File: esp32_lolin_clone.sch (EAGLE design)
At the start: 33 parts, among them J1 10104111-0001LF, P1 S2B-PH-SM4-TB, Q1 CJ2301S1, Q2 CJ2301S1, SW1 PTS815SJK250SMTR, U1 ESP32-WROOM-32D, U2 BCM857, U3 ME6211, U4 UMH3N, U5 TP4054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

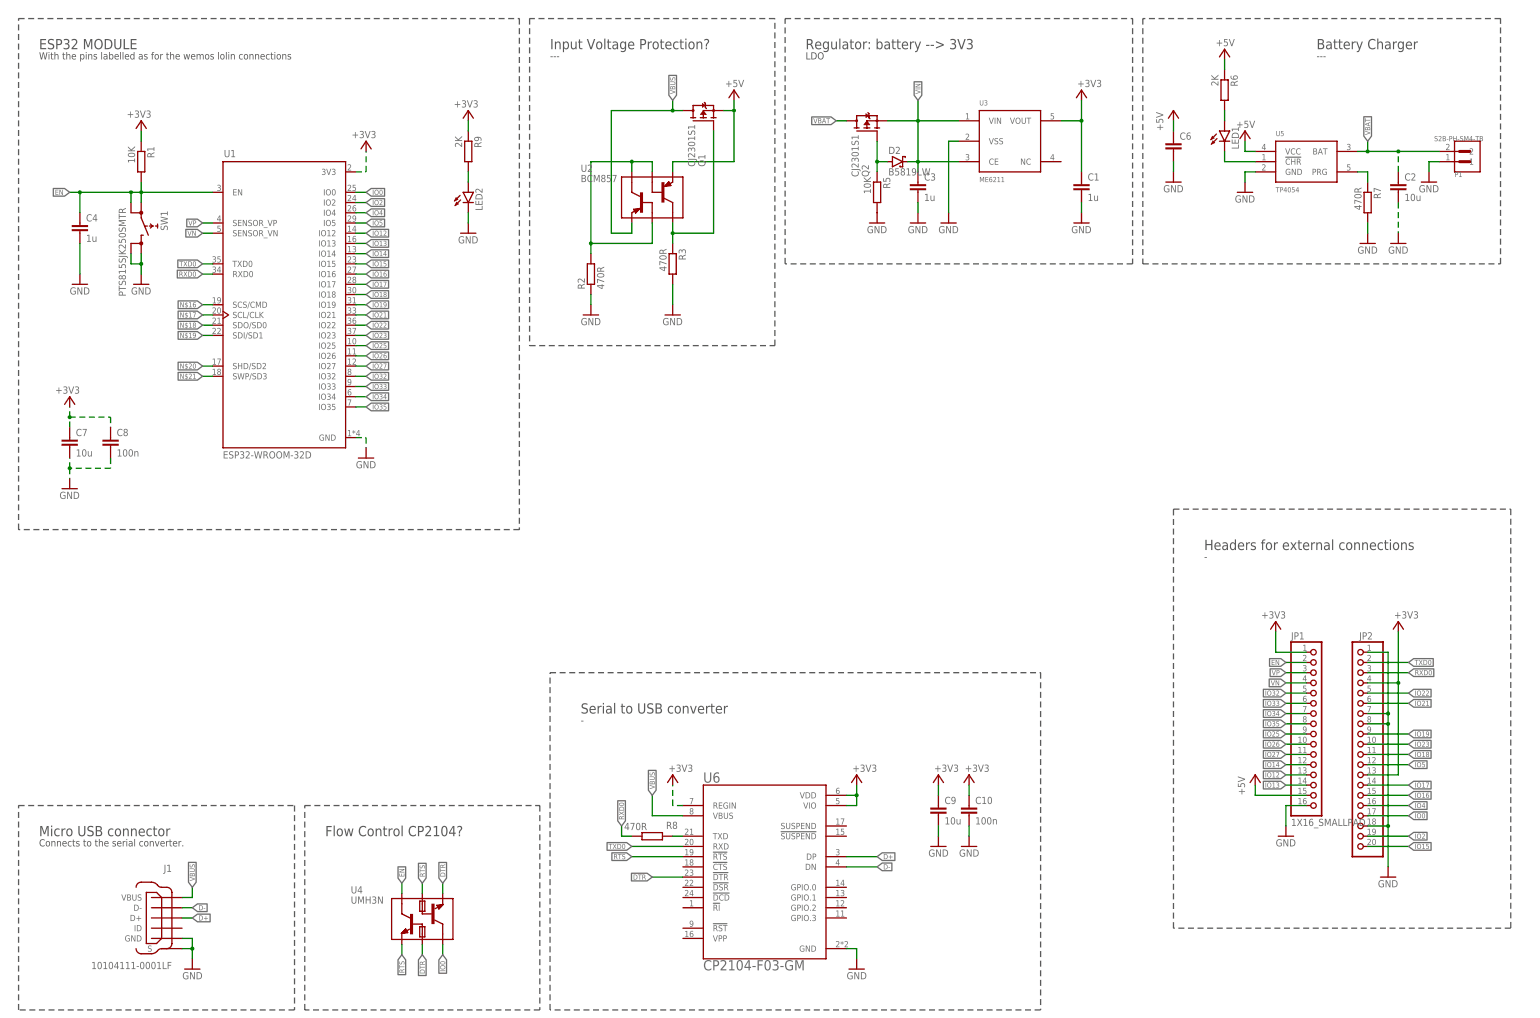
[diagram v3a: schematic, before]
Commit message: - Finish BOM, modify BOM related issues in schematic.
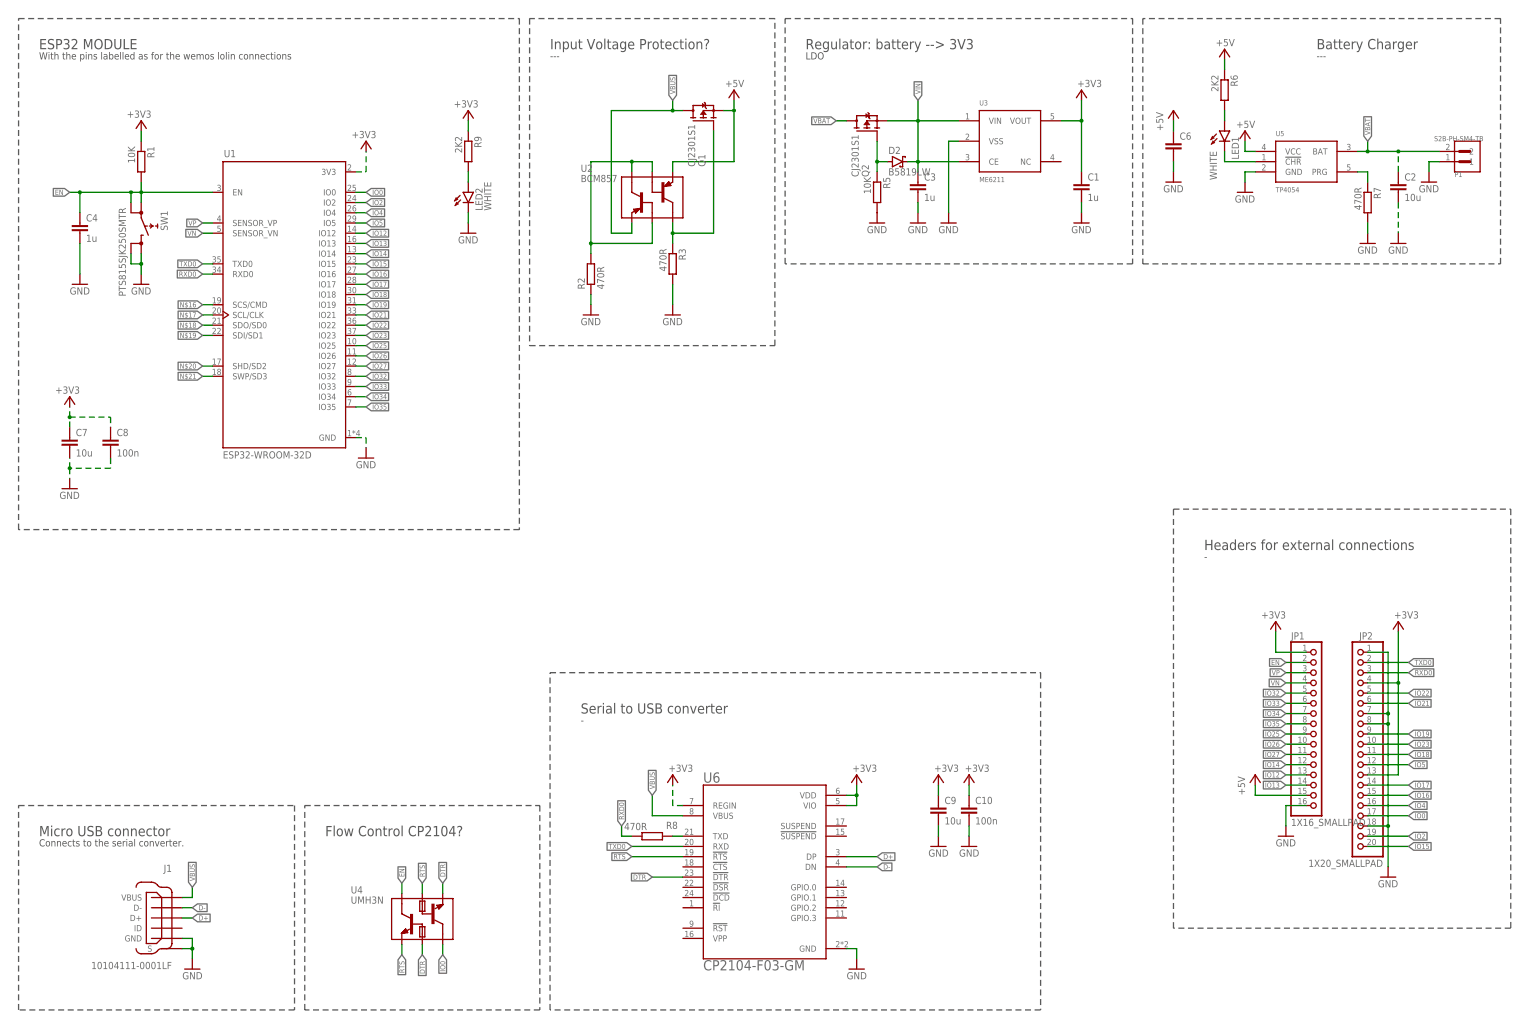
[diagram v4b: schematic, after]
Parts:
- JP2: value (none) -> 1X20_SMALLPAD; device RE_wemos_lolin_clone:PINHD-1X20 -> RE_wemos_lolin_clone:1X20_SMALLPAD
- LED1, LED2: value (none) -> WHITE
- R6, R9: value 2K -> 2K2
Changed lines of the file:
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@@
 <part name="U6" library="RE_wemos_lolin_clone" deviceset="CP2104" device="-F03-GM"/>
 <part name="R8" library="rcl" library_urn="urn:adsk.eagle:library:334" deviceset="R-EU_" device="R0603" package3d_urn="urn:adsk.eagle:package:23555/3" value="470R"/>
-<part name="LED2" library="led" library_urn="urn:adsk.eagle:library:259" deviceset="LED" device="CHIP-LED0603" package3d_urn="urn:adsk.eagle:package:15819/3"/>
-<part name="R9" library="rcl" library_urn="urn:adsk.eagle:library:334" deviceset="R-EU_" device="R0603" package3d_urn="urn:adsk.eagle:package:23555/3" value="2K"/>
+<part name="LED2" library="led" library_urn="urn:adsk.eagle:library:259" deviceset="LED" device="CHIP-LED0603" package3d_urn="urn:adsk.eagle:package:15819/3" value="WHITE"/>
+<part name="R9" library="rcl" library_urn="urn:adsk.eagle:library:334" deviceset="R-EU_" device="R0603" package3d_urn="urn:adsk.eagle:package:23555/3" value="2K2"/>
 <part name="GND1" library="supply1" library_urn="urn:adsk.eagle:library:371" deviceset="GND" device=""/>
 <part name="+3V1" library="supply1" library_urn="urn:adsk.eagle:library:371" deviceset="+3V3" device=""/>
 <part name="C10" library="rcl" library_urn="urn:adsk.eagle:library:334" deviceset="C-EU" device="C0603K" package3d_urn="urn:adsk.eagle:package:23680/2" value="100n"/>
 <part name="JP1" library="RE_wemos_lolin_clone" deviceset="1X16_SMALLPAD" device=""/>
-<part name="JP2" library="RE_wemos_lolin_clone" deviceset="PINHD-1X20" device="" package3d_urn="urn:adsk.eagle:package:22441/2"/>
+<part name="JP2" library="RE_wemos_lolin_clone" deviceset="1X20_SMALLPAD" device=""/>
 <part name="GND2" library="supply1" library_urn="urn:adsk.eagle:library:371" deviceset="GND" device=""/>
 <part name="+3V2" library="supply1" library_urn="urn:adsk.eagle:library:371" deviceset="+3V3" device=""/>
@@
 <part name="GND15" library="supply1" library_urn="urn:adsk.eagle:library:371" deviceset="GND" device=""/>
 <part name="+3V7" library="supply1" library_urn="urn:adsk.eagle:library:371" deviceset="+3V3" device=""/>
-<part name="LED1" library="led" library_urn="urn:adsk.eagle:library:259" deviceset="LED" device="CHIP-LED0603" package3d_urn="urn:adsk.eagle:package:15819/3"/>
-<part name="R6" library="rcl" library_urn="urn:adsk.eagle:library:334" deviceset="R-EU_" device="R0603" package3d_urn="urn:adsk.eagle:package:23555/3" value="2K"/>
+<part name="LED1" library="led" library_urn="urn:adsk.eagle:library:259" deviceset="LED" device="CHIP-LED0603" package3d_urn="urn:adsk.eagle:package:15819/3" value="WHITE"/>
+<part name="R6" library="rcl" library_urn="urn:adsk.eagle:library:334" deviceset="R-EU_" device="R0603" package3d_urn="urn:adsk.eagle:package:23555/3" value="2K2"/>
 <part name="P+3" library="supply1" library_urn="urn:adsk.eagle:library:371" deviceset="+5V" device=""/>
 <part name="GND16" library="supply1" library_urn="urn:adsk.eagle:library:371" deviceset="GND" device=""/>
@@
 <attribute name="VALUE" x="323.85" y="53.34" size="1.778" layer="96"/>
 </instance>
-<instance part="JP2" gate="A" x="340.36" y="73.66" smashed="yes" rot="MR0">
+<instance part="JP2" gate="G$1" x="340.36" y="73.66" smashed="yes" rot="MR0">
 <attribute name="NAME" x="344.17" y="99.695" size="1.778" layer="95" rot="MR0"/>
 <attribute name="VALUE" x="346.71" y="43.18" size="1.778" layer="96" rot="MR0"/>
@@
 </instance>
 <instance part="LED1" gate="G$1" x="307.34" y="226.06" smashed="yes">
-<attribute name="NAME" x="310.896" y="221.488" size="1.778" layer="95" rot="R90"/>
-<attribute name="VALUE" x="313.055" y="221.488" size="1.778" layer="96" rot="R90"/>
+<attribute name="NAME" x="310.896" y="218.948" size="1.778" layer="95" rot="R90"/>
+<attribute name="VALUE" x="305.435" y="213.868" size="1.778" layer="96" rot="R90"/>
 </instance>
 <instance part="R6" gate="G$1" x="307.34" y="236.22" smashed="yes" rot="R270">
@@
 </segment>
 <segment>
-<pinref part="JP2" gate="A" pin="2"/>
+<pinref part="JP2" gate="G$1" pin="2"/>
 <wire x1="342.9" y1="93.98" x2="353.06" y2="93.98" width="0.1524" layer="91"/>
 <label x="353.06" y="93.98" size="1.27" layer="95" xref="yes"/>
@@
 </segment>
 <segment>
-<pinref part="JP2" gate="A" pin="3"/>
+<pinref part="JP2" gate="G$1" pin="3"/>
 <wire x1="342.9" y1="91.44" x2="353.06" y2="91.44" width="0.1524" layer="91"/>
 <label x="353.06" y="91.44" size="1.27" layer="95" xref="yes"/>
@@
 </segment>
 <segment>
-<pinref part="JP2" gate="A" pin="4"/>
+<pinref part="JP2" gate="G$1" pin="4"/>
 <wire x1="342.9" y1="88.9" x2="350.52" y2="88.9" width="0.1524" layer="91"/>
 <wire x1="350.52" y1="88.9" x2="350.52" y2="101.6" width="0.1524" layer="91"/>
-<pinref part="JP2" gate="A" pin="13"/>
+<pinref part="JP2" gate="G$1" pin="13"/>
 <wire x1="342.9" y1="66.04" x2="350.52" y2="66.04" width="0.1524" layer="91"/>
 <wire x1="350.52" y1="66.04" x2="350.52" y2="88.9" width="0.1524" layer="91"/>
@@
 </segment>
 <segment>
-<pinref part="JP2" gate="A" pin="1"/>
+<pinref part="JP2" gate="G$1" pin="1"/>
 <wire x1="342.9" y1="96.52" x2="347.98" y2="96.52" width="0.1524" layer="91"/>
 <pinref part="GND3" gate="1" pin="GND"/>
 <wire x1="347.98" y1="96.52" x2="347.98" y2="81.28" width="0.1524" layer="91"/>
-<pinref part="JP2" gate="A" pin="7"/>
+<pinref part="JP2" gate="G$1" pin="7"/>
 <wire x1="347.98" y1="81.28" x2="347.98" y2="78.74" width="0.1524" layer="91"/>
 <wire x1="347.98" y1="78.74" x2="347.98" y2="53.34" width="0.1524" layer="91"/>
@@
 <wire x1="342.9" y1="81.28" x2="347.98" y2="81.28" width="0.1524" layer="91"/>
 <junction x="347.98" y="81.28"/>
-<pinref part="JP2" gate="A" pin="8"/>
+<pinref part="JP2" gate="G$1" pin="8"/>
 <wire x1="342.9" y1="78.74" x2="347.98" y2="78.74" width="0.1524" layer="91"/>
 <junction x="347.98" y="78.74"/>
-<pinref part="JP2" gate="A" pin="18"/>
+<pinref part="JP2" gate="G$1" pin="18"/>
 <wire x1="342.9" y1="53.34" x2="347.98" y2="53.34" width="0.1524" layer="91"/>
 <junction x="347.98" y="53.34"/>
@@
 <net name="IO22" class="0">
 <segment>
-<pinref part="JP2" gate="A" pin="5"/>
+<pinref part="JP2" gate="G$1" pin="5"/>
 <wire x1="342.9" y1="86.36" x2="353.06" y2="86.36" width="0.1524" layer="91"/>
 <label x="353.06" y="86.36" size="1.27" layer="95" xref="yes"/>
@@
 <net name="IO21" class="0">
 <segment>
-<pinref part="JP2" gate="A" pin="6"/>
+<pinref part="JP2" gate="G$1" pin="6"/>
 <wire x1="342.9" y1="83.82" x2="353.06" y2="83.82" width="0.1524" layer="91"/>
 <label x="353.06" y="83.82" size="1.27" layer="95" xref="yes"/>
@@
 <net name="IO19" class="0">
 <segment>
-<pinref part="JP2" gate="A" pin="9"/>
+<pinref part="JP2" gate="G$1" pin="9"/>
 <wire x1="342.9" y1="76.2" x2="353.06" y2="76.2" width="0.1524" layer="91"/>
 <label x="353.06" y="76.2" size="1.27" layer="95" xref="yes"/>
@@
 <net name="IO23" class="0">
 <segment>
-<pinref part="JP2" gate="A" pin="10"/>
+<pinref part="JP2" gate="G$1" pin="10"/>
 <wire x1="342.9" y1="73.66" x2="353.06" y2="73.66" width="0.1524" layer="91"/>
 <label x="353.06" y="73.66" size="1.27" layer="95" xref="yes"/>
@@
 <net name="IO18" class="0">
 <segment>
-<pinref part="JP2" gate="A" pin="11"/>
+<pinref part="JP2" gate="G$1" pin="11"/>
 <wire x1="342.9" y1="71.12" x2="353.06" y2="71.12" width="0.1524" layer="91"/>
 <label x="353.06" y="71.12" size="1.27" layer="95" xref="yes"/>
@@
 <net name="IO5" class="0">
 <segment>
-<pinref part="JP2" gate="A" pin="12"/>
+<pinref part="JP2" gate="G$1" pin="12"/>
 <wire x1="342.9" y1="68.58" x2="353.06" y2="68.58" width="0.1524" layer="91"/>
 <label x="353.06" y="68.58" size="1.27" layer="95" xref="yes"/>
@@
 <net name="IO17" class="0">
 <segment>
-<pinref part="JP2" gate="A" pin="14"/>
+<pinref part="JP2" gate="G$1" pin="14"/>
 <wire x1="342.9" y1="63.5" x2="353.06" y2="63.5" width="0.1524" layer="91"/>
 <label x="353.06" y="63.5" size="1.27" layer="95" xref="yes"/>
@@
 <net name="IO16" class="0">
 <segment>
-<pinref part="JP2" gate="A" pin="15"/>
+<pinref part="JP2" gate="G$1" pin="15"/>
 <wire x1="342.9" y1="60.96" x2="353.06" y2="60.96" width="0.1524" layer="91"/>
 <label x="353.06" y="60.96" size="1.27" layer="95" xref="yes"/>
@@
 <net name="IO4" class="0">
 <segment>
-<pinref part="JP2" gate="A" pin="16"/>
+<pinref part="JP2" gate="G$1" pin="16"/>
 <wire x1="342.9" y1="58.42" x2="353.06" y2="58.42" width="0.1524" layer="91"/>
 <label x="353.06" y="58.42" size="1.27" layer="95" xref="yes"/>
@@
 <net name="IO0" class="0">
 <segment>
-<pinref part="JP2" gate="A" pin="17"/>
+<pinref part="JP2" gate="G$1" pin="17"/>
 <wire x1="342.9" y1="55.88" x2="353.06" y2="55.88" width="0.1524" layer="91"/>
 <label x="353.06" y="55.88" size="1.27" layer="95" xref="yes"/>
@@
 <net name="IO2" class="0">
 <segment>
-<pinref part="JP2" gate="A" pin="19"/>
+<pinref part="JP2" gate="G$1" pin="19"/>
 <wire x1="342.9" y1="50.8" x2="353.06" y2="50.8" width="0.1524" layer="91"/>
 <label x="353.06" y="50.8" size="1.27" layer="95" xref="yes"/>
@@
 <net name="IO15" class="0">
 <segment>
-<pinref part="JP2" gate="A" pin="20"/>
+<pinref part="JP2" gate="G$1" pin="20"/>
 <wire x1="342.9" y1="48.26" x2="353.06" y2="48.26" width="0.1524" layer="91"/>
 <label x="353.06" y="48.26" size="1.27" layer="95" xref="yes"/>

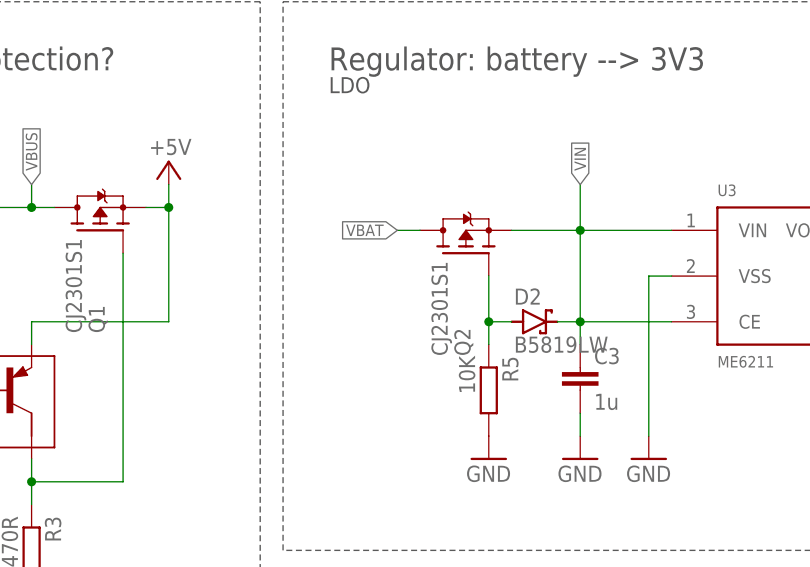
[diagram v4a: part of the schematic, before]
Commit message: - Fix critical error 5V connection missing.
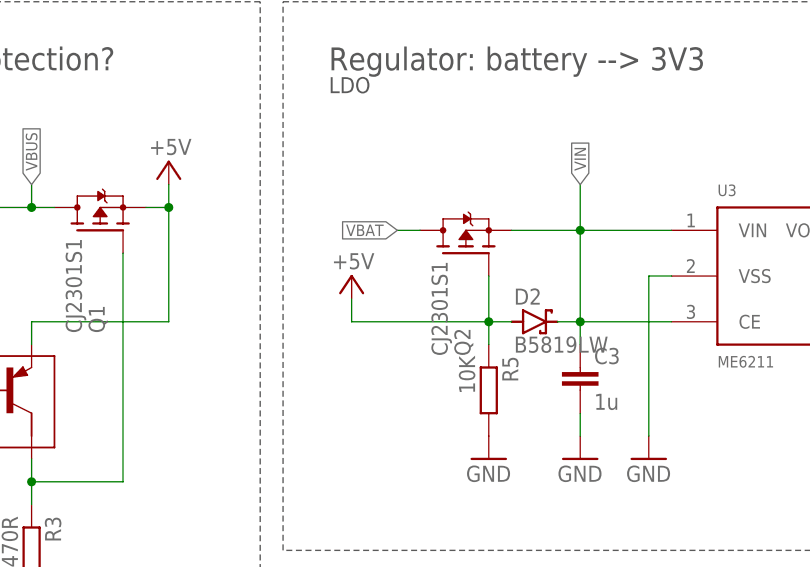
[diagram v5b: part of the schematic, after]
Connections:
- removed net N$5: D2.A, Q2.G, R5.1
- net +5V: now also D2.A, Q2.G, R5.1
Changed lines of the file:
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@@
 <part name="GND22" library="supply1" library_urn="urn:adsk.eagle:library:371" deviceset="GND" device=""/>
 <part name="+3V11" library="supply1" library_urn="urn:adsk.eagle:library:371" deviceset="+3V3" device=""/>
+<part name="P+6" library="supply1" library_urn="urn:adsk.eagle:library:371" deviceset="+5V" device=""/>
 </parts>
 <sheets>
@@
 <attribute name="VALUE" x="175.26" y="68.58" size="1.778" layer="96" rot="R180"/>
 </instance>
+<instance part="P+6" gate="1" x="205.74" y="223.52" smashed="yes">
+<attribute name="VALUE" x="208.28" y="226.06" size="1.778" layer="96" rot="R180"/>
+</instance>
 </instances>
 <busses>
@@
 <junction x="185.42" y="231.14"/>
 </segment>
+<segment>
+<pinref part="D2" gate="G$1" pin="A"/>
+<wire x1="223.52" y1="218.44" x2="220.98" y2="218.44" width="0.1524" layer="91"/>
+<pinref part="R5" gate="G$1" pin="1"/>
+<wire x1="220.98" y1="218.44" x2="220.98" y2="215.9" width="0.1524" layer="91"/>
+<pinref part="Q2" gate="G$1" pin="G"/>
+<wire x1="220.98" y1="218.44" x2="220.98" y2="223.52" width="0.1524" layer="91"/>
+<junction x="220.98" y="218.44"/>
+<wire x1="220.98" y1="218.44" x2="205.74" y2="218.44" width="0.1524" layer="91"/>
+<wire x1="205.74" y1="218.44" x2="205.74" y2="220.98" width="0.1524" layer="91"/>
+<pinref part="P+6" gate="1" pin="+5V"/>
+</segment>
 </net>
 <net name="IO2" class="0">
@@
 </segment>
 </net>
-<net name="N$5" class="0">
-<segment>
-<pinref part="D2" gate="G$1" pin="A"/>
-<wire x1="223.52" y1="218.44" x2="220.98" y2="218.44" width="0.1524" layer="91"/>
-<pinref part="R5" gate="G$1" pin="1"/>
-<wire x1="220.98" y1="218.44" x2="220.98" y2="215.9" width="0.1524" layer="91"/>
-<pinref part="Q2" gate="G$1" pin="G"/>
-<wire x1="220.98" y1="218.44" x2="220.98" y2="223.52" width="0.1524" layer="91"/>
-<junction x="220.98" y="218.44"/>
-</segment>
-</net>

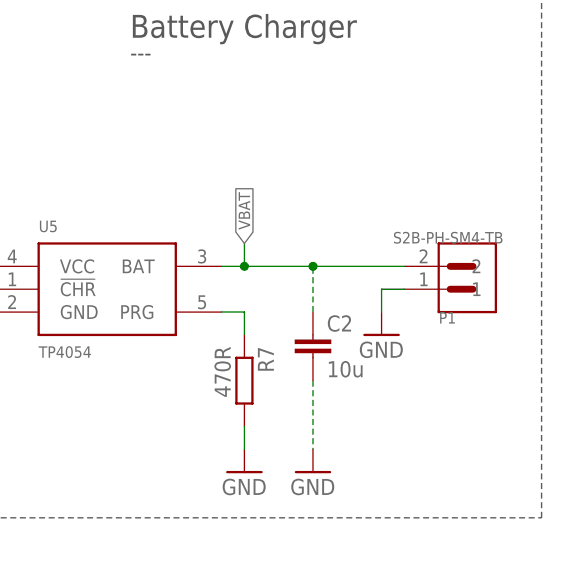
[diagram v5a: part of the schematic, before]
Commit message: - Change device reference BCM857, so it really matches the footprint at the board.
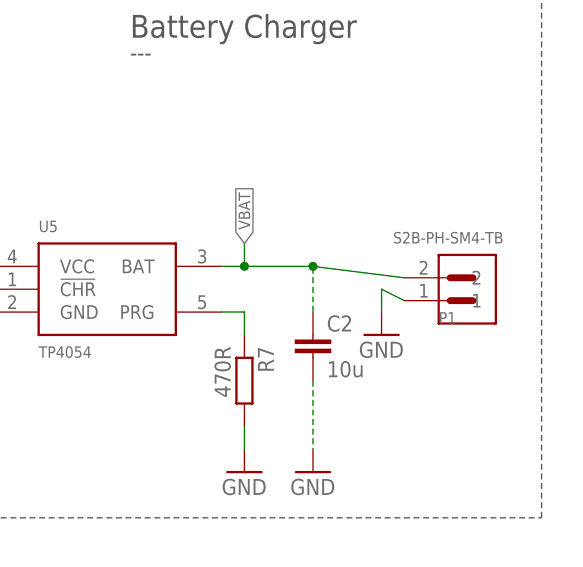
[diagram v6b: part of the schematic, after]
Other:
- moved on the sheet: P1
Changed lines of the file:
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@@
 <segment>
 <pinref part="P1" gate="G$1" pin="1"/>
-<wire x1="360.68" y1="218.44" x2="358.14" y2="218.44" width="0.1524" layer="91"/>
+<wire x1="360.68" y1="217.17" x2="358.14" y2="218.44" width="0.1524" layer="91"/>
 <wire x1="358.14" y1="218.44" x2="358.14" y2="215.9" width="0.1524" layer="91"/>
 <pinref part="GND12" gate="1" pin="GND"/>
@@
 <label x="342.9" y="223.52" size="1.27" layer="95" rot="R90" xref="yes"/>
 <pinref part="P1" gate="G$1" pin="2"/>
-<wire x1="360.68" y1="220.98" x2="350.52" y2="220.98" width="0.1524" layer="91"/>
+<wire x1="360.68" y1="219.71" x2="350.52" y2="220.98" width="0.1524" layer="91"/>
 <junction x="342.9" y="220.98"/>
 <pinref part="C2" gate="G$1" pin="1"/>
